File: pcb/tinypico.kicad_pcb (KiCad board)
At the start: 2 copper layers, 19 x 14.1 mm, 9 parts, among them J1 Conn_01x05_Pin, J2 Conn_01x05_Pin, U1 ATtiny202-SS

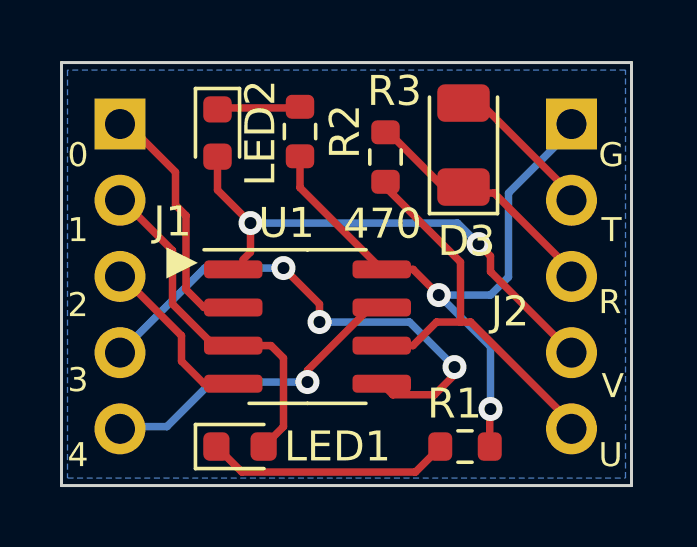
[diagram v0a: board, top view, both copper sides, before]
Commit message: 回路図のリファクタリング
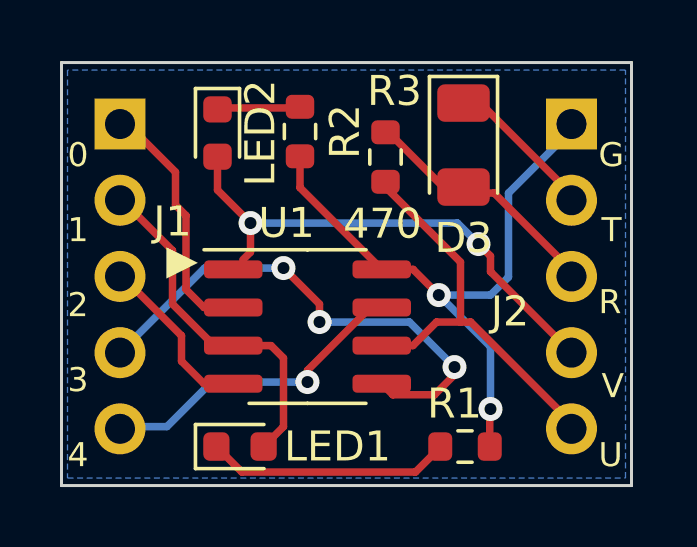
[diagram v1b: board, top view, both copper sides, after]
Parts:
- LED1: value LED -> LED_G
- LED2: value LED -> LED_R
- turned D3 to -90 degrees
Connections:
- D3 pad 1: UPDI_RX -> UPDI_TX
- D3 pad 2: UPDI_TX -> UPDI_RX
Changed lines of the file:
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@@
   (net 2 "3")
   (net 3 "4")
-  (net 4 "Net-(D1-K)")
-  (net 5 "Net-(D2-K)")
+  (net 4 "Net-(LED1-K)")
+  (net 5 "Net-(LED2-K)")
   (net 6 "8")
   (net 7 "5")
@@
       (stroke (width 0.1) (type solid)) (layer "F.Fab"))
     (pad "1" smd roundrect (at -0.825 0 270) (size 0.8 0.95) (layers "F.Cu" "F.Paste" "F.Mask") (roundrect_rratio 0.25)
-      (net 5 "Net-(D2-K)") (pintype "passive"))
+      (net 5 "Net-(LED2-K)") (pintype "passive"))
     (pad "2" smd roundrect (at 0.825 0 270) (size 0.8 0.95) (layers "F.Cu" "F.Paste" "F.Mask") (roundrect_rratio 0.25)
       (net 6 "8") (pintype "passive"))
@@
   )
   (footprint "Diode_SMD:D_1206_3216Metric" (layer "F.Cu")
-    (at 99.2 73.7 90)
+    (at 99.2 73.7 -90)
     (descr "Diode SMD 1206 (3216 Metric), square (rectangular) end terminal, IPC_7351 nominal, (Body size source: http://www.tortai-tech.com/upload/download/2011102023233369053.pdf), generated with kicad-footprint-generator")
     (tags "diode")
@@
     (property "ki_keywords" "diode")
     (attr smd)
-    (fp_text reference "D3" (at -3.2 0.1) (layer "F.SilkS")
+    (fp_text reference "D3" (at 3.1 0) (layer "F.SilkS")
         (effects (font (size 1 1) (thickness 0.15)))
     )
@@
     (fp_line (start 1.6 0.8) (end 1.6 -0.8)
       (stroke (width 0.1) (type solid)) (layer "F.Fab"))
-    (pad "1" smd roundrect (at -1.4 0 90) (size 1.25 1.75) (layers "F.Cu" "F.Paste" "F.Mask") (roundrect_rratio 0.2)
-      (net 11 "UPDI_RX") (pinfunction "K") (pintype "passive"))
-    (pad "2" smd roundrect (at 1.4 0 90) (size 1.25 1.75) (layers "F.Cu" "F.Paste" "F.Mask") (roundrect_rratio 0.2)
-      (net 12 "UPDI_TX") (pinfunction "A") (pintype "passive"))
+    (pad "1" smd roundrect (at -1.4 0 270) (size 1.25 1.75) (layers "F.Cu" "F.Paste" "F.Mask") (roundrect_rratio 0.2)
+      (net 12 "UPDI_TX") (pinfunction "K") (pintype "passive"))
+    (pad "2" smd roundrect (at 1.4 0 270) (size 1.25 1.75) (layers "F.Cu" "F.Paste" "F.Mask") (roundrect_rratio 0.2)
+      (net 11 "UPDI_RX") (pinfunction "A") (pintype "passive"))
     (model "${KICAD6_3DMODEL_DIR}/Diode_SMD.3dshapes/D_1206_3216Metric.wrl"
       (offset (xyz 0 0 0))
@@
       (stroke (width 0.1) (type solid)) (layer "F.Fab"))
     (pad "1" smd roundrect (at -0.825 0) (size 0.8 0.95) (layers "F.Cu" "F.Paste" "F.Mask") (roundrect_rratio 0.25)
-      (net 4 "Net-(D1-K)") (pintype "passive"))
+      (net 4 "Net-(LED1-K)") (pintype "passive"))
     (pad "2" smd roundrect (at 0.825 0) (size 0.8 0.95) (layers "F.Cu" "F.Paste" "F.Mask") (roundrect_rratio 0.25)
       (net 6 "8") (pintype "passive"))
@@
         (effects (font (size 1 1) (thickness 0.15)))
     )
-    (fp_text value "LED" (at 0 2.25) (layer "F.Fab")
+    (fp_text value "LED_G" (at 0 2.25) (layer "F.Fab")
         (effects (font (size 1 1) (thickness 0.15)))
     )
@@
       (stroke (width 0.1) (type solid)) (layer "F.Fab"))
     (pad "1" smd roundrect (at -0.7875 0) (size 0.875 0.95) (layers "F.Cu" "F.Paste" "F.Mask") (roundrect_rratio 0.25)
-      (net 4 "Net-(D1-K)") (pinfunction "K") (pintype "passive"))
+      (net 4 "Net-(LED1-K)") (pinfunction "K") (pintype "passive"))
     (pad "2" smd roundrect (at 0.7875 0) (size 0.875 0.95) (layers "F.Cu" "F.Paste" "F.Mask") (roundrect_rratio 0.25)
       (net 2 "3") (pinfunction "A") (pintype "passive"))
@@
         (effects (font (size 1 1) (thickness 0.15)))
     )
-    (fp_text value "LED" (at -3.3 0.5) (layer "F.Fab")
+    (fp_text value "LED_R" (at -3.3 0.5) (layer "F.Fab")
         (effects (font (size 1 1) (thickness 0.15)))
     )
@@
       (stroke (width 0.1) (type solid)) (layer "F.Fab"))
     (pad "1" smd roundrect (at -0.7875 0 270) (size 0.875 0.95) (layers "F.Cu" "F.Paste" "F.Mask") (roundrect_rratio 0.25)
-      (net 5 "Net-(D2-K)") (pinfunction "K") (pintype "passive"))
+      (net 5 "Net-(LED2-K)") (pinfunction "K") (pintype "passive"))
     (pad "2" smd roundrect (at 0.7875 0 270) (size 0.875 0.95) (layers "F.Cu" "F.Paste" "F.Mask") (roundrect_rratio 0.25)
       (net 10 "1") (pinfunction "A") (pintype "passive"))
